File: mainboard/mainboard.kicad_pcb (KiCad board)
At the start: 2 copper layers, 70 x 100 mm, 72 parts, among them J17 Conn_01x10_Female, J18 Conn_01x10_Female, J7 Eurorack_Power, Q1 2N3906, Q2 2N3904, Q3 2N3906, Q4 2N3904, U1 40106, U2 TL074, U3 TL074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

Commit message: Changed mounting holes
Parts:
- moved R16 7.18 mm to (19.7, 23.3)
- moved R18 6.07 mm to (27.3, 20.8), turned to 180 degrees
- moved U1 5.00 mm to (31.1, 3.98)
- moved U4 5.00 mm to (31.1, 25.1)
- moved C10 5.00 mm to (24.5, 34.5)
- moved C11 5.00 mm to (3.25, 44.1)
- moved C12 5.00 mm to (8.25, 36.0)
- moved C13 5.00 mm to (8.50, 74.8)
- moved C16 5.00 mm to (59.0, 7.85)
- moved C17 5.00 mm to (48.2, 34.5)
- moved C18 5.00 mm to (66.8, 44.1)
- moved C19 5.00 mm to (61.8, 36.0)
- moved C20 5.00 mm to (61.5, 74.8)
- moved C3 5.00 mm to (44.5, 84.0)
- moved C4 5.00 mm to (25.0, 84.0)
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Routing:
- net Net-(D5-Pad1): track 8.24 -> 17.9 mm
- net CLK_IN_1: track 37.6 -> 32.4 mm
- net RATE_SEL_1: track 72.4 -> 75.4 mm
- net Net-(R16-Pad1): track 16.1 -> 18.8 mm
- net Net-(D5-Pad2): track 26.8 -> 25.9 mm
- net IN_1: track 50.6 -> 49.9 mm
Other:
- outline, holes or cut-outs redrawn

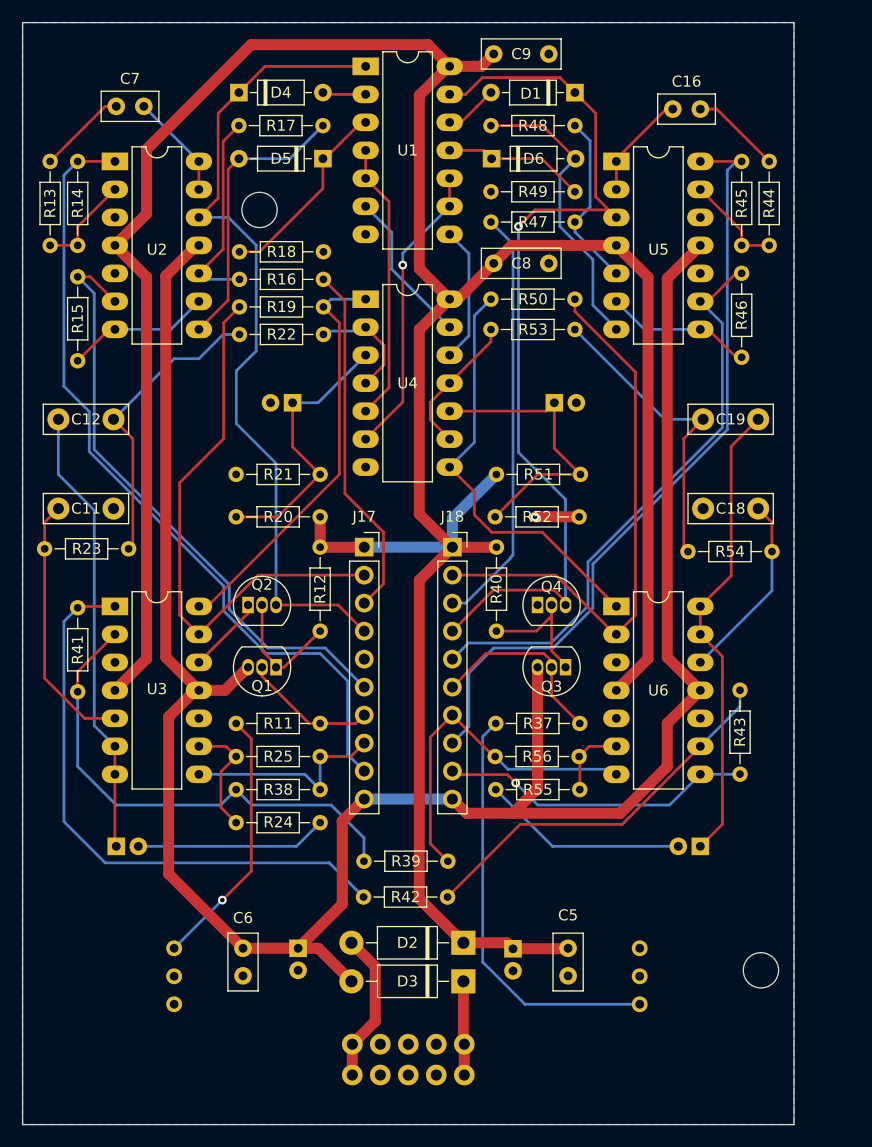
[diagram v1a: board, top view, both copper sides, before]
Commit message: Changed mounting holes
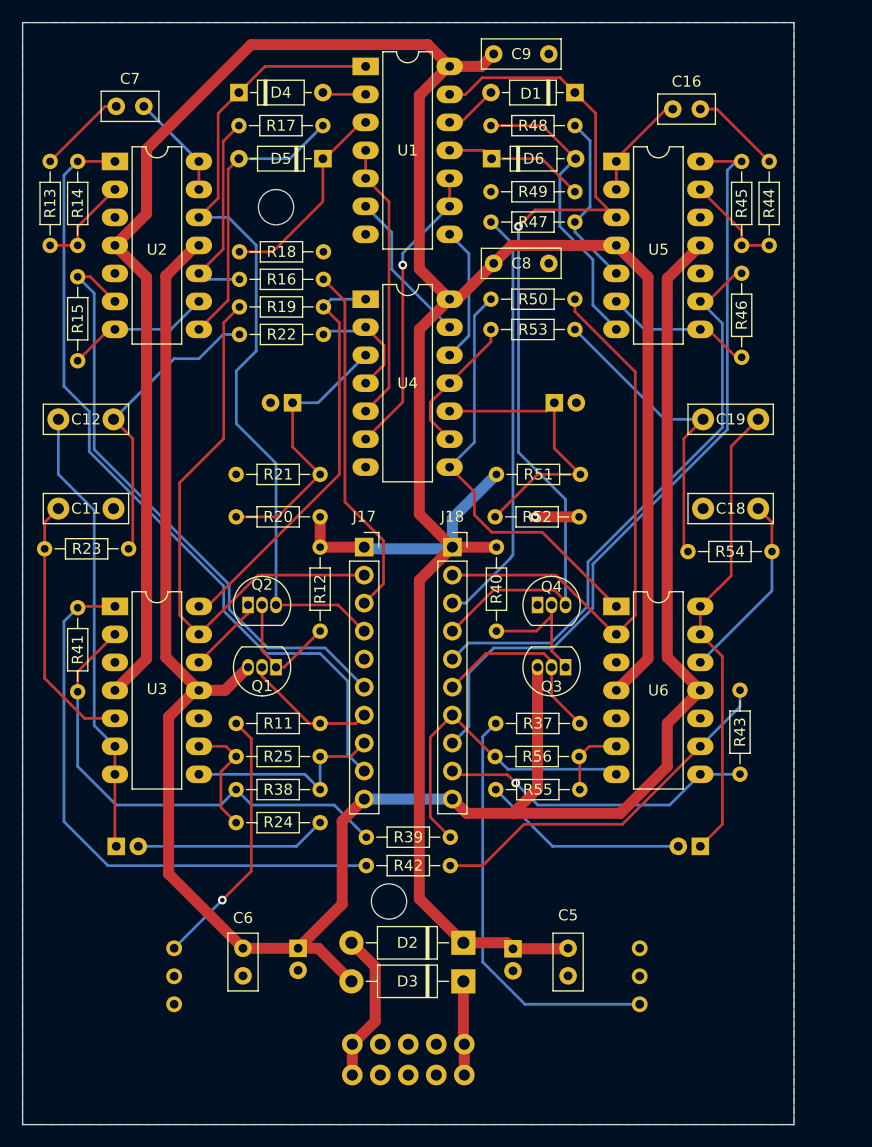
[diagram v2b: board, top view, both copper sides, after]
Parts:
- moved R42 2.86 mm to (38.8, 76.5)
- moved R39 2.19 mm to (31.2, 73.9)
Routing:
- net OUT_2: track 31.9 -> 29.8 mm
- net Net-(R38-Pad1): track 45.3 -> 43.4 mm
- net Net-(R42-Pad1): track 35.2 -> 33.8 mm
- net Net-(R41-Pad1): track 53.4 -> 52.4 mm
- net Net-(D5-Pad1): track 17.9 -> 18.6 mm
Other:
- outline, holes or cut-outs redrawn
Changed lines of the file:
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@@
   )
   (footprint "Resistor_THT:R_Axial_DIN0204_L3.6mm_D1.6mm_P7.62mm_Horizontal" (layer "F.Cu")
-    (at 30.975 76.1)
+    (at 31.19 73.92)
     (descr "Resistor, Axial_DIN0204 series, Axial, Horizontal, pin pitch=7.62mm, 0.167W, length*diameter=3.6*1.6mm^2, http://cdn-reichelt.de/documents/datenblatt/B400/1_4W%23YAG.pdf")
     (tags "Resistor Axial_DIN0204 series Axial Horizontal pin pitch 7.62mm 0.167W length 3.6mm diameter 1.6mm")
@@
   )
   (footprint "Resistor_THT:R_Axial_DIN0204_L3.6mm_D1.6mm_P7.62mm_Horizontal" (layer "F.Cu")
-    (at 38.56 79.35 180)
+    (at 38.81 76.5 180)
     (descr "Resistor, Axial_DIN0204 series, Axial, Horizontal, pin pitch=7.62mm, 0.167W, length*diameter=3.6*1.6mm^2, http://cdn-reichelt.de/documents/datenblatt/B400/1_4W%23YAG.pdf")
     (tags "Resistor Axial_DIN0204 series Axial Horizontal pin pitch 7.62mm 0.167W length 3.6mm diameter 1.6mm")
@@
     )
   )
-  (gr_circle (center 21.5 17) (end 23.1 17) (layer "Edge.Cuts") (width 0.1) (fill none))
-  (gr_circle (center 67 86) (end 68.6 86) (layer "Edge.Cuts") (width 0.1) (fill none))
+  (gr_circle (center 23 16.75) (end 24.6 16.75) (layer "Edge.Cuts") (width 0.1) (fill none))
+  (gr_circle (center 33.25 79.75) (end 34.85 79.75) (layer "Edge.Cuts") (width 0.1) (fill none))
   (gr_rect (start 0 0) (end 70 100) (layer "Edge.Cuts") (width 0.1) (fill none))
   (gr_rect (start 0 0) (end 70 100) (layer "User.2") (width 0.15) (fill none))
@@
   (segment (start 8.38 20.22) (end 11.25 23.09) (width 1) (layer "F.Cu") (net 1))
   (segment (start 39 47.6) (end 39 45) (width 1) (layer "B.Cu") (net 1))
+  (segment (start 39 47.6) (end 38.85 47.75) (width 1) (layer "B.Cu") (net 1))
   (segment (start 39 45) (end 43 41) (width 1) (layer "B.Cu") (net 1))
-  (segment (start 39 47.6) (end 31 47.6) (width 1) (layer "B.Cu") (net 1))
+  (segment (start 38.85 47.75) (end 31.15 47.75) (width 1) (layer "B.Cu") (net 1))
+  (segment (start 31.15 47.75) (end 31 47.6) (width 1) (layer "B.Cu") (net 1))
   (segment (start 16 58.055) (end 20.46 53.595) (width 0.25) (layer "F.Cu") (net 2))
   (segment (start 50.5 44.85) (end 46.5 44.850001) (width 1) (layer "F.Cu") (net 2))
@@
   (segment (start 27.415 6.515) (end 27.25 6.35) (width 0.25) (layer "F.Cu") (net 23))
   (segment (start 31.13 6.515) (end 27.415 6.515) (width 0.25) (layer "F.Cu") (net 23))
-  (segment (start 21.497044 20.8) (end 27.25 15.047044) (width 0.25) (layer "F.Cu") (net 24))
+  (segment (start 27.25 16.25) (end 27.25 12.35) (width 0.25) (layer "F.Cu") (net 24))
   (segment (start 27.25 12.35) (end 27.435 12.35) (width 0.25) (layer "F.Cu") (net 24))
   (segment (start 30.73 9.055) (end 31.13 9.055) (width 0.25) (layer "F.Cu") (net 24))
-  (segment (start 19.68 20.8) (end 21.497044 20.8) (width 0.25) (layer "F.Cu") (net 24))
-  (segment (start 27.25 15.047044) (end 27.25 12.35) (width 0.25) (layer "F.Cu") (net 24))
+  (segment (start 22.7 20.8) (end 27.25 16.25) (width 0.25) (layer "F.Cu") (net 24))
+  (segment (start 19.68 20.8) (end 22.7 20.8) (width 0.25) (layer "F.Cu") (net 24))
   (segment (start 27.435 12.35) (end 30.73 9.055) (width 0.25) (layer "F.Cu") (net 24))
   (segment (start 18.655 13.325) (end 19.63 12.35) (width 0.25) (layer "F.Cu") (net 25))
@@
   (segment (start 16 55.515) (end 21.375 50.14) (width 0.25) (layer "F.Cu") (net 28))
   (segment (start 18.25 27.23) (end 19.68 25.8) (width 0.25) (layer "F.Cu") (net 28))
+  (segment (start 32.75 47) (end 29.25 43.5) (width 0.25) (layer "F.Cu") (net 29))
   (segment (start 31 52.68) (end 32.75 50.93) (width 0.25) (layer "F.Cu") (net 29))
-  (segment (start 29.25 42.75) (end 29.25 25.25) (width 0.25) (layer "F.Cu") (net 29))
   (segment (start 29.25 25.25) (end 27.3 23.3) (width 0.25) (layer "F.Cu") (net 29))
-  (segment (start 32.75 50.93) (end 32.75 46.25) (width 0.25) (layer "F.Cu") (net 29))
-  (segment (start 32.75 46.25) (end 29.25 42.75) (width 0.25) (layer "F.Cu") (net 29))
+  (segment (start 29.25 43.5) (end 29.25 25.25) (width 0.25) (layer "F.Cu") (net 29))
+  (segment (start 32.75 50.93) (end 32.75 47) (width 0.25) (layer "F.Cu") (net 29))
   (segment (start 6.145 23.065) (end 8.38 25.3) (width 0.25) (layer "F.Cu") (net 30))
   (segment (start 5 23.065) (end 6.145 23.065) (width 0.25) (layer "F.Cu") (net 30))
@@
   (segment (start 48 61.04) (end 48 58.5) (width 0.25) (layer "F.Cu") (net 37))
   (segment (start 47.3 57.25) (end 48 57.95) (width 0.25) (layer "F.Cu") (net 37))
-  (segment (start 38.595 76.1) (end 37 74.505) (width 0.25) (layer "F.Cu") (net 38))
+  (segment (start 38.81 73.92) (end 37 72.11) (width 0.25) (layer "F.Cu") (net 38))
   (segment (start 39 62.84) (end 42.76 66.6) (width 0.25) (layer "F.Cu") (net 38))
+  (segment (start 37 72.11) (end 37 64.84) (width 0.25) (layer "F.Cu") (net 38))
   (segment (start 37 64.84) (end 39 62.84) (width 0.25) (layer "F.Cu") (net 38))
   (segment (start 42.76 66.6) (end 42.88 66.6) (width 0.25) (layer "F.Cu") (net 38))
-  (segment (start 37 74.505) (end 37 64.84) (width 0.25) (layer "F.Cu") (net 38))
   (segment (start 53.88 68.215) (end 53.415 67.75) (width 0.25) (layer "B.Cu") (net 38))
   (segment (start 53.415 67.75) (end 44.03 67.75) (width 0.25) (layer "B.Cu") (net 38))
@@
   (segment (start 5 58.895) (end 8.38 55.515) (width 0.25) (layer "F.Cu") (net 51))
   (segment (start 5 60.72) (end 5 58.895) (width 0.25) (layer "F.Cu") (net 51))
-  (segment (start 20.78 71) (end 28 71) (width 0.25) (layer "B.Cu") (net 51))
+  (segment (start 19.38 69.6) (end 20.78 71) (width 0.25) (layer "B.Cu") (net 51))
   (segment (start 8.5 71) (end 17.98 71) (width 0.25) (layer "B.Cu") (net 51))
   (segment (start 17.98 71) (end 19.38 69.6) (width 0.25) (layer "B.Cu") (net 51))
   (segment (start 5 67.5) (end 8.5 71) (width 0.25) (layer "B.Cu") (net 51))
-  (segment (start 19.38 69.6) (end 20.78 71) (width 0.25) (layer "B.Cu") (net 51))
-  (segment (start 30.975 73.975) (end 30.975 76.1) (width 0.25) (layer "B.Cu") (net 51))
-  (segment (start 28 71) (end 30.975 73.975) (width 0.25) (layer "B.Cu") (net 51))
+  (segment (start 28.27 71) (end 31.19 73.92) (width 0.25) (layer "B.Cu") (net 51))
+  (segment (start 20.78 71) (end 28.27 71) (width 0.25) (layer "B.Cu") (net 51))
   (segment (start 5 60.72) (end 5 67.5) (width 0.25) (layer "B.Cu") (net 51))
   (segment (start 8.38 52.975) (end 5.125 52.975) (width 0.25) (layer "F.Cu") (net 52))
   (segment (start 5.125 52.975) (end 5 53.1) (width 0.25) (layer "F.Cu") (net 52))
   (segment (start 3.75 72.5) (end 3.75 54.35) (width 0.25) (layer "B.Cu") (net 52))
-  (segment (start 30.94 79.35) (end 27.84 76.25) (width 0.25) (layer "B.Cu") (net 52))
-  (segment (start 27.84 76.25) (end 7.5 76.25) (width 0.25) (layer "B.Cu") (net 52))
   (segment (start 3.75 54.35) (end 5 53.1) (width 0.25) (layer "B.Cu") (net 52))
-  (segment (start 7.5 76.25) (end 3.75 72.5) (width 0.25) (layer "B.Cu") (net 52))
-  (segment (start 45.16 72.75) (end 54.425 72.75) (width 0.25) (layer "F.Cu") (net 53))
+  (segment (start 31.19 76.5) (end 7.75 76.5) (width 0.25) (layer "B.Cu") (net 52))
+  (segment (start 7.75 76.5) (end 3.75 72.5) (width 0.25) (layer "B.Cu") (net 52))
+  (segment (start 38.81 76.5) (end 41.75 76.5) (width 0.25) (layer "F.Cu") (net 53))
+  (segment (start 41.75 76.5) (end 45.5 72.75) (width 0.25) (layer "F.Cu") (net 53))
   (segment (start 54.425 72.75) (end 61.5 65.675) (width 0.25) (layer "F.Cu") (net 53))
-  (segment (start 38.56 79.35) (end 45.16 72.75) (width 0.25) (layer "F.Cu") (net 53))
+  (segment (start 45.5 72.75) (end 54.425 72.75) (width 0.25) (layer "F.Cu") (net 53))
   (segment (start 65.1 62.075) (end 65.1 60.58) (width 0.25) (layer "B.Cu") (net 53))
   (segment (start 61.5 65.675) (end 65.1 62.075) (width 0.25) (layer "B.Cu") (net 53))
